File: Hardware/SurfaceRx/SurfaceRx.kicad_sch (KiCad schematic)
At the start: 33 parts, among them IC1 SC189ZSKTRT, J1 Conn_01x03, J2 Conn_01x03, J3 Conn_01x03, J4 Conn_01x03, J5 Conn_01x03, J6 Conn_01x03, J7 Conn_01x05, J8 Conn_01x03, P1 VDD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

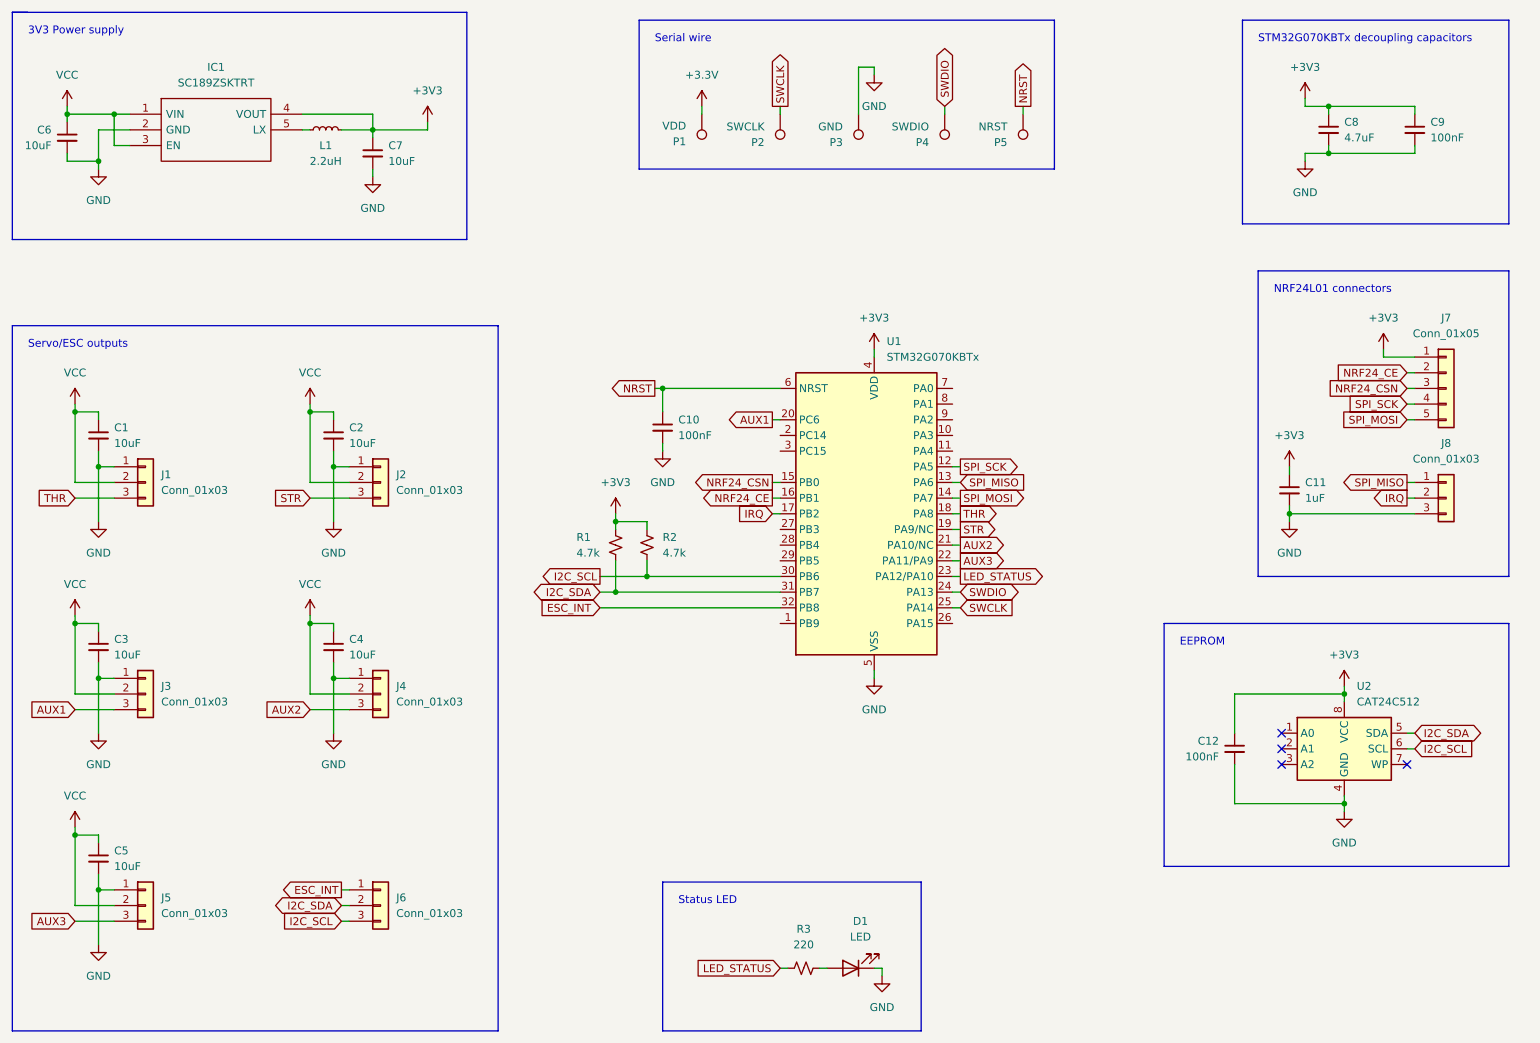
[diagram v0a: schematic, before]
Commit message: Modified PCB layout
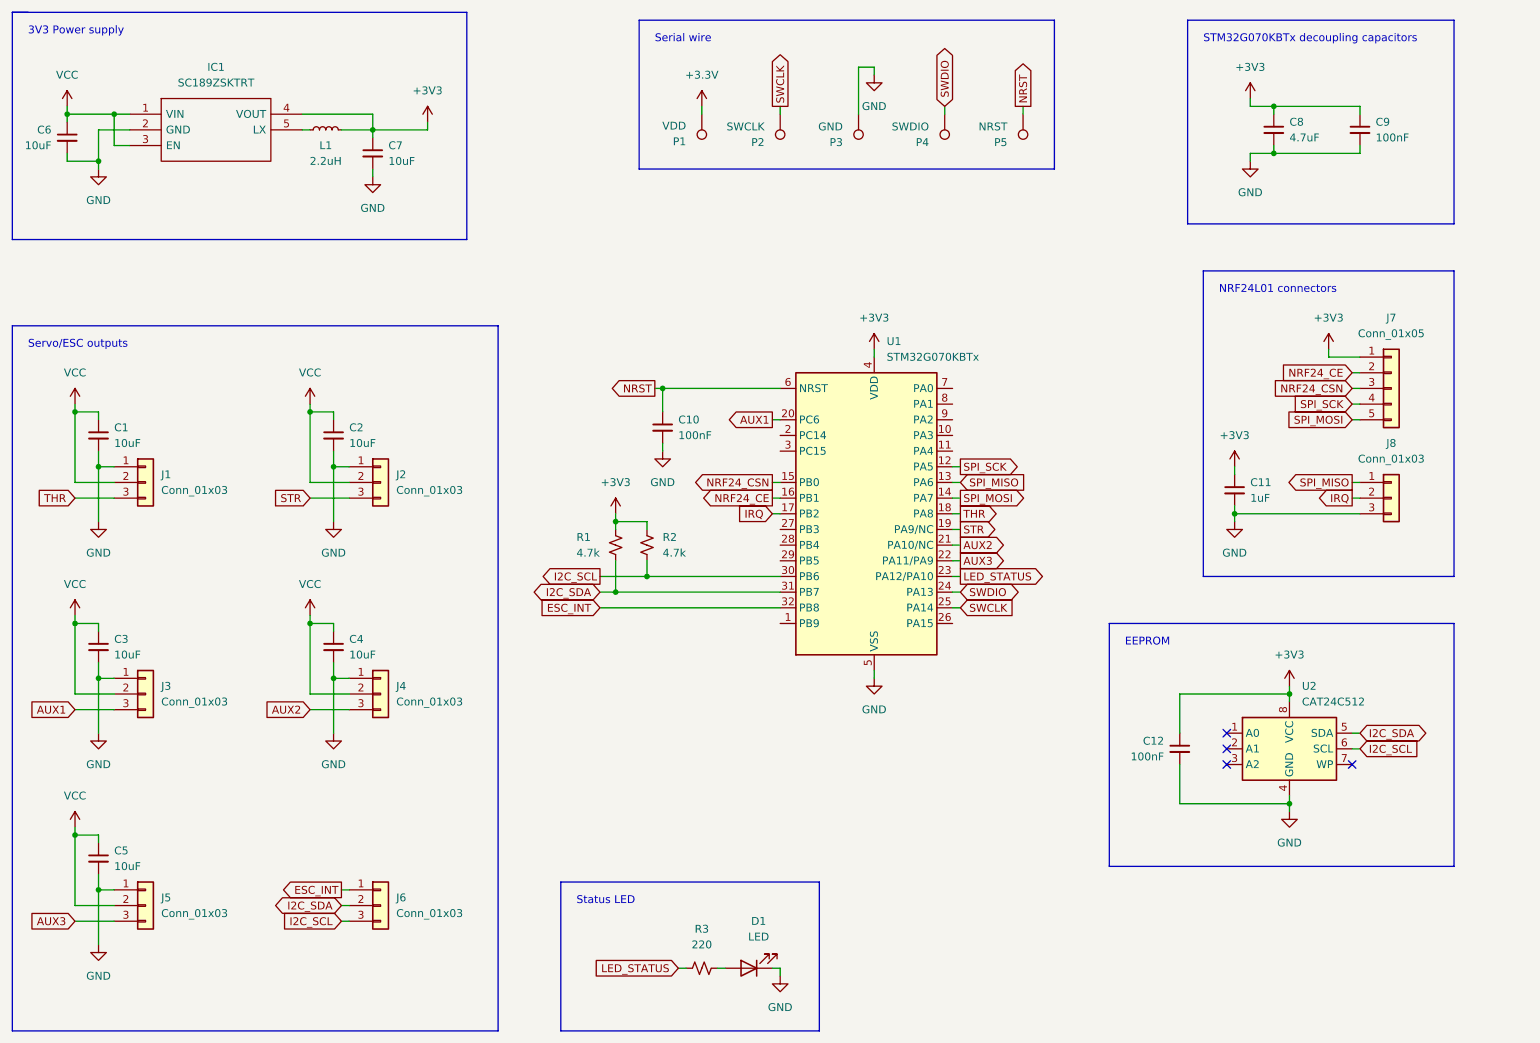
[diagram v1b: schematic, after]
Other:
- moved on the sheet: C11, C12, C8, C9, D1, J7, J8, R3, U2

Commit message: Corrected net name for SWD 3V3 pin
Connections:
- net +3.3V is gone; now on net +3V3: P1.1
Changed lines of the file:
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@@
     (pin "2")
-  )
-  (symbol (lib_id "power:+3.3V") (at 133.35 35.56 0) (unit 1)
-    (in_bom yes) (on_board yes) (fields_autoplaced)
-    (property "Reference" "#PWR025" (id 0) (at 133.35 39.37 0)
-      (effects (font (size 1.27 1.27)) hide)
-    )
-    (property "Value" "+3.3V" (id 1) (at 133.35 30.48 0))
-    (property "Footprint" "" (id 2) (at 133.35 35.56 0)
-      (effects (font (size 1.27 1.27)) hide)
-    )
-    (property "Datasheet" "" (id 3) (at 133.35 35.56 0)
-      (effects (font (size 1.27 1.27)) hide)
-    )
-    (pin "1")
   )
   (symbol (lib_id "SamacSys_Parts:SC189ZSKTRT") (at 40.64 36.83 0) (unit 1)
@@
     (pin "4")
     (pin "5")
+  )
+  (symbol (lib_id "power:+3V3") (at 133.35 35.56 0) (unit 1)
+    (in_bom yes) (on_board yes) (fields_autoplaced)
+    (property "Reference" "#PWR?" (id 0) (at 133.35 39.37 0)
+      (effects (font (size 1.27 1.27)) hide)
+    )
+    (property "Value" "+3V3" (id 1) (at 133.35 30.48 0))
+    (property "Footprint" "" (id 2) (at 133.35 35.56 0)
+      (effects (font (size 1.27 1.27)) hide)
+    )
+    (property "Datasheet" "" (id 3) (at 133.35 35.56 0)
+      (effects (font (size 1.27 1.27)) hide)
+    )
+    (pin "1")
   )
   (symbol (lib_id "Device:C_Small") (at 35.56 88.9 0) (unit 1)
@@
       (reference "#PWR024") (unit 1) (value "GND") (footprint "")
     )
-    (path "/ad1419c2-9990-43c0-9e56-20874596dc66"
-      (reference "#PWR025") (unit 1) (value "+3.3V") (footprint "")
-    )
     (path "/3d32942a-0988-4c8f-9a97-511c45fce17f"
       (reference "#PWR026") (unit 1) (value "+3V3") (footprint "")
@@
       (reference "#PWR028") (unit 1) (value "GND") (footprint "")
     )
+    (path "/b44bb049-8e8d-4ecc-97a0-ff118a632ec2"
+      (reference "#PWR?") (unit 1) (value "+3V3") (footprint "")
+    )
     (path "/b8979e0e-732a-478b-a779-b8fe0478ee1c"

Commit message: Added reference designators on PCB for SMD components only. Changed designator from 'IC1' to 'U3'.
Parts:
- renumbered IC1 to U3
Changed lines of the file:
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@@
   (symbol (lib_id "SamacSys_Parts:SC189ZSKTRT") (at 40.64 36.83 0) (unit 1)
     (in_bom yes) (on_board yes) (fields_autoplaced)
-    (property "Reference" "IC1" (id 0) (at 54.61 29.21 0))
+    (property "Reference" "U3" (id 0) (at 54.61 29.21 0))
     (property "Value" "SC189ZSKTRT" (id 1) (at 54.61 31.75 0))
     (property "Footprint" "SamacSys_Parts:SOT95P280X145-5N" (id 2) (at 64.77 34.29 0)
@@
       (reference "D1") (unit 1) (value "LED") (footprint "LED_SMD:LED_0603_1608Metric")
     )
-    (path "/addc6cf4-b4f5-4c59-b37c-65bd4167e7d9"
-      (reference "IC1") (unit 1) (value "SC189ZSKTRT") (footprint "SamacSys_Parts:SOT95P280X145-5N")
-    )
     (path "/6d28bcac-71e6-4094-bc46-8032e6c34cab"
       (reference "J1") (unit 1) (value "Conn_01x03") (footprint "Connector_PinHeader_2.54mm:PinHeader_1x03_P2.54mm_Vertical")
@@
       (reference "U2") (unit 1) (value "CAT24C512") (footprint "Package_SO:TSSOP-8_4.4x3mm_P0.65mm")
     )
-  )
+    (path "/addc6cf4-b4f5-4c59-b37c-65bd4167e7d9"
+      (reference "U3") (unit 1) (value "SC189ZSKTRT") (footprint "SamacSys_Parts:SOT95P280X145-5N")
+    )
+  )
